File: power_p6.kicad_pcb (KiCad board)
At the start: 4 copper layers, 44.8 x 41.5 mm, 23 parts, among them J1 LSHM-140-04.0-L-DV-A-N-K-TR, U1 LT8624S

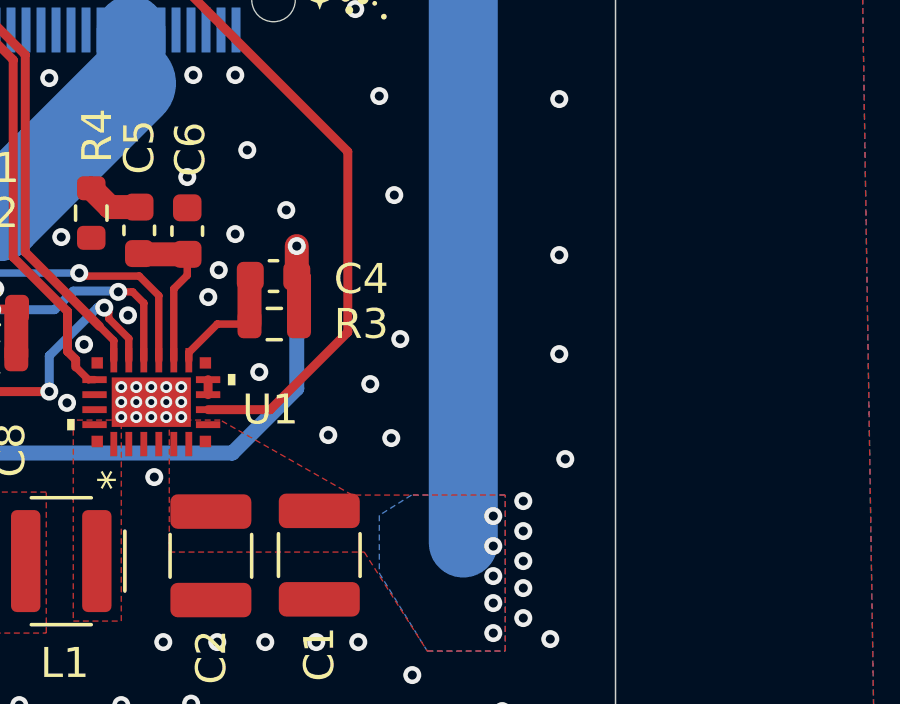
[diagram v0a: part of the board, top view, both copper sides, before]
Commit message: Add input RC snubber
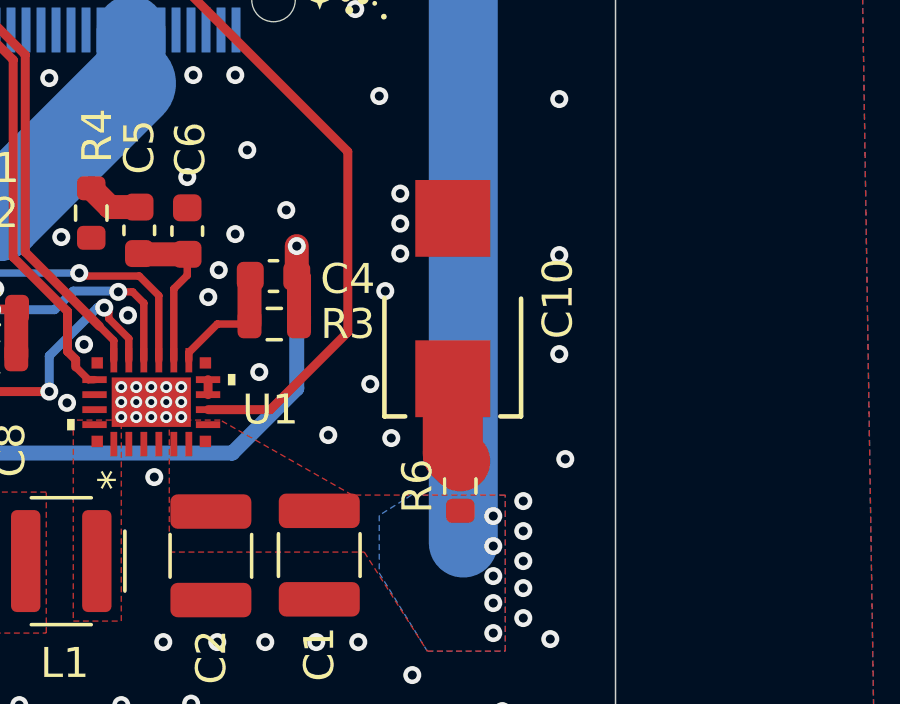
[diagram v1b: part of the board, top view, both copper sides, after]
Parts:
- added C10: 100u, lib:T521X, F.Cu at (139.8, 55.2)
- added R6: 0.5, Resistor_SMD:R_0603_1608Metric, F.Cu at (140.0, 61.5)
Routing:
- net /cf1: track 0.00 -> 2.86 mm
- net GND: vias 153 -> 155

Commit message: Update
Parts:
- U1: value LT8624S -> 05-08-1602_Rev_A_ADI

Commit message: update set resistor to thin film
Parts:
- R3: value 59k -> 60.4k
- U1: value 05-08-1602_Rev_A_ADI -> LT8624S
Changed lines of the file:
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@@
 			)
 		)
-		(property "Value" "59k"
+		(property "Value" "60.4k"
 			(at 0 1.43 0)
 			(layer "F.Fab")
@@
 			)
 		)
-		(property "Description" "59 kOhms ±1% 0.1W, 1/10W Chip Resistor 0603 (1608 Metric) Automotive AEC-Q200 Thick Film"
-			(at 0 0 0)
-			(layer "F.Fab")
-			(hide yes)
-			(effects
-				(font
-					(size 1.27 1.27)
-					(thickness 0.15)
-				)
-			)
-		)
-		(property "M" "Vishay"
-			(at 0 0 0)
-			(unlocked yes)
-			(layer "F.Fab")
-			(hide yes)
-			(effects
-				(font
-					(size 1 1)
-					(thickness 0.15)
-				)
-			)
-		)
-		(property "MPN" "CRCW060359K0FKEA"
-			(at 0 0 0)
-			(unlocked yes)
-			(layer "F.Fab")
-			(hide yes)
-			(effects
-				(font
-					(size 1 1)
-					(thickness 0.15)
-				)
-			)
-		)
-		(property "Field6" ""
+		(property "Description" "60.4 kOhms ±0.1% 0.1W, 1/10W Chip Resistor 0603 (1608 Metric) Automotive AEC-Q200 Thin Film"
+			(at 0 0 0)
+			(layer "F.Fab")
+			(hide yes)
+			(effects
+				(font
+					(size 1.27 1.27)
+					(thickness 0.15)
+				)
+			)
+		)
+		(property "M" "Panasonic"
+			(at 0 0 0)
+			(unlocked yes)
+			(layer "F.Fab")
+			(hide yes)
+			(effects
+				(font
+					(size 1 1)
+					(thickness 0.15)
+				)
+			)
+		)
+		(property "MPN" "ERA-3AEB6042V"
 			(at 0 0 0)
 			(unlocked yes)
@@
 			)
 		)
-		(property "Value" "05-08-1602_Rev_A_ADI"
+		(property "Value" "LT8624S"
 			(at 0 0 90)
 			(unlocked yes)
